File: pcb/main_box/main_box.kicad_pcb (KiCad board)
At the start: 2 copper layers, 150 x 70 mm, 21 parts, among them J1 AudioJack4_SwitchTR1, J2 AudioJack4_SwitchTR1, J3 AudioJack4_SwitchTR1, J4 AudioJack4_SwitchTR1, J5 AudioJack4_SwitchTR1, J6 AudioJack4_SwitchTR1, J7 AudioJack4_SwitchTR1, J8 AudioJack4_SwitchTR1, J9 Conn_01x05_MountingPin, SW1 SW_Push, SW2 SW_Push, SW3 SW_Push, SW4 SW_Push, SW5 SW_Push, SW6 SW_Push, U1 Pico

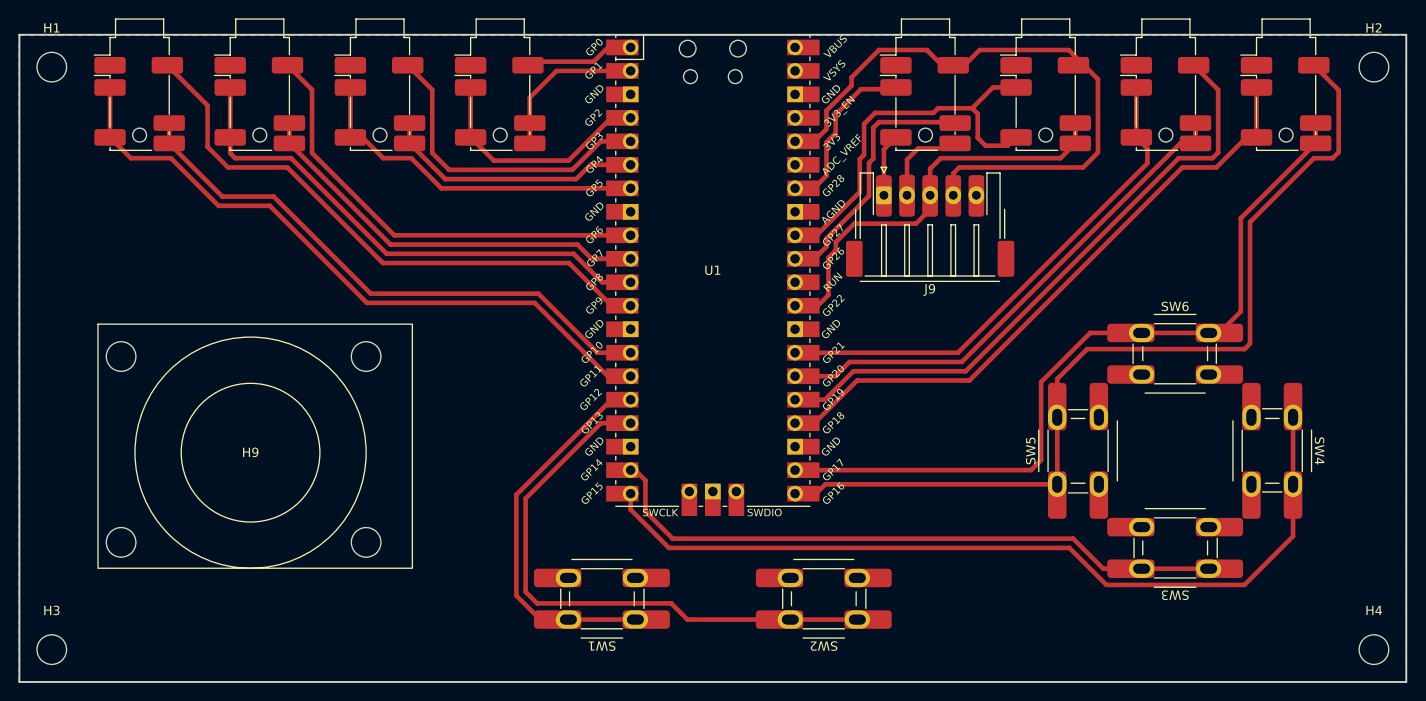
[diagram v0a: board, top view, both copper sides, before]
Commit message: Had to speedrun changing footprint of jacks, laskakit had wrong part number on their site...
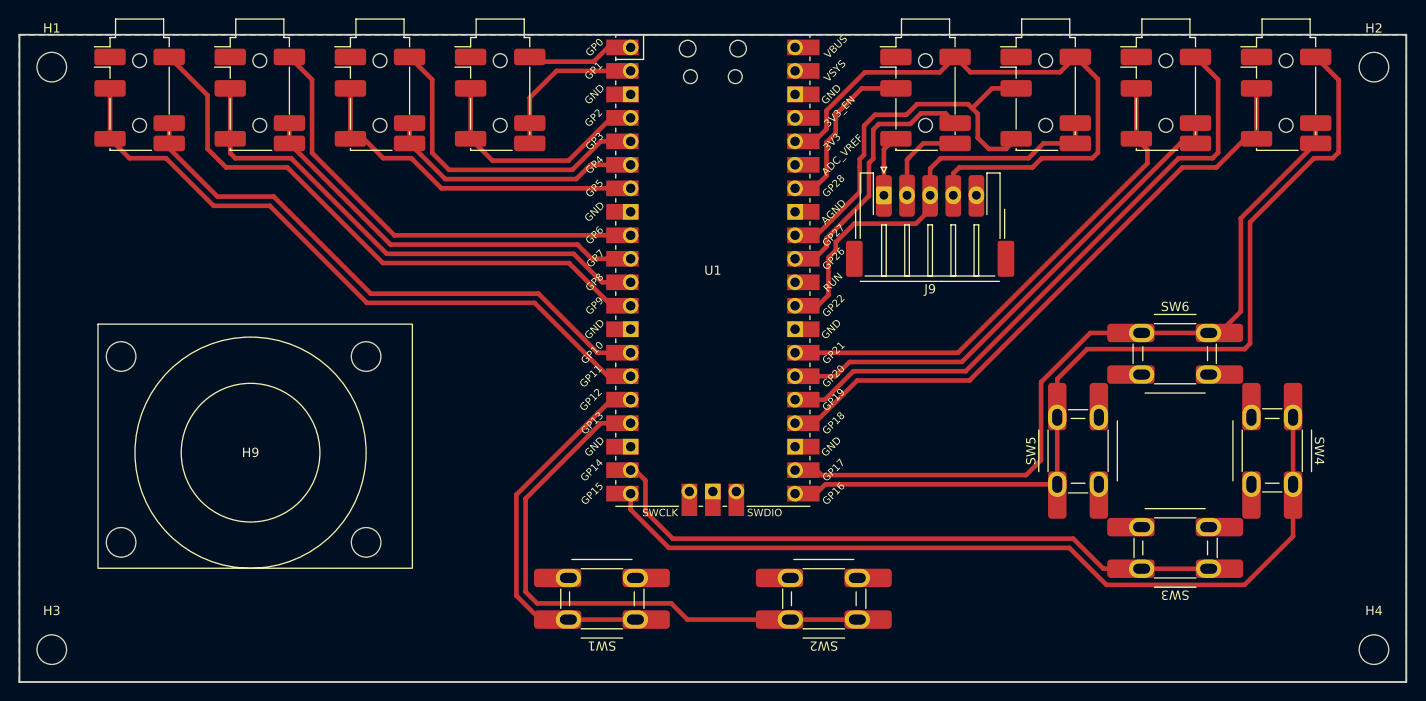
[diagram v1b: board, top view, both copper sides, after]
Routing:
- net +3V3: track 68.2 -> 67.2 mm
- net /GPIO9: track 63.5 -> 64.5 mm
- net /GPIO16: track 99.0 -> 99.8 mm
- net /GPIO19: track 67.4 -> 68.2 mm
- net /GPIO6: track 48.7 -> 49.5 mm
- net /GPIO3: track 34.1 -> 34.9 mm
- net /ADC0: track 28.1 -> 28.8 mm
